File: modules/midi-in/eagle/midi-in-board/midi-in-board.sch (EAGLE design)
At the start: 20 parts, among them IC1 LM358N, T1 BC547, T2 BC547, X1 MIDI IN, X2 MIDI THRU

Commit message: Finish up midi in board schematic, for now
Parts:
- added C2, C3, C4, C5, C6, C7: 100n, rcl:C-EU050-024X044
- added IC2: TL072P, linear:TL072P
- added IC3, IC4: TL074P, linear:TL074P
- added JP1, JP2: (no value), pinhead:PINHD-1X8
- added JP3: (no value), pinhead:PINHD-1X1
- added JP4: (no value), pinhead:PINHD-1X7
- added JP5, JP6: (no value), pinhead:PINHD-1X2
- added R10, R12, R13, R14, R15, R16, R18, R20, R22, R24, R26, R27, R33, R35, R37, R39, R41, R49, R50, R9: 10K, rcl:R-EU_0207/7
- added R11: 1K, rcl:R-EU_0207/7
- added R17, R19, R21, R23, R25, R28, R29, R30, R31, R32: 100K, rcl:R-EU_0207/7
- added R34, R36, R38, R40, R42: 3.6K, rcl:R-EU_0207/7
- added R43, R44, R45, R46, R47, R51: 1K, pot:TRIM_EU-CA6V
- added R48: 20K, rcl:R-EU_0207/7
- added R52, R53: 220R, rcl:R-EU_0207/7
- added T3: BC547, transistor:BC547
- added X3: CHANNEL SELECT SW, con-molex:22-23-2021
- added X4: POWER IN, con-wago-500:W237-103
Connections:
- new net N$13: C3.1, R12.1, R17.1, SV2.12
- new net N$27: IC2A.-IN, R17.2, R28.1
- new net N$28: IC3A.-IN, R19.2, R29.1
- new net N$29: IC3C.-IN, R21.2, R30.1
- new net N$30: C2.2, R10.2, V11.!SRCLR, V21.!SRCLR
- new net N$31: IC4A.-IN, R23.2, R31.1
- new net N$32: IC4C.-IN, R25.2, R32.1
- new net N$33: IC2A.OUT, R18.1, R28.2
- new net N$34: IC2B.-IN, R18.2, R33.1
- new net N$35: IC3A.OUT, R20.1, R29.2
- new net N$36: IC3B.-IN, R20.2, R35.1
- new net N$37: IC3C.OUT, R22.1, R30.2
- new net N$38: IC3D.-IN, R22.2, R37.1
- new net N$39: IC4C.OUT, R27.1, R32.2
- new net N$40: IC4D.-IN, R27.2, R41.1
- new net N$41: IC2P.V-, IC3P.V-, X4-3.KL
- new net N$42: R50.2, R51.A
- new net N$43: IC4P.V-
- new net N$44: R48.1, R49.2
- new net N$45: R49.1, R51.E
- new net N$46: IC2A.+IN, IC3A.+IN, IC3C.+IN, IC4A.+IN, IC4C.+IN, R51.S
- new net N$48: JP1.1, V11.QA
- new net N$49: JP1.2, V11.QB
- new net N$50: JP1.3, V11.QC
- new net N$51: JP1.4, V11.QD
- new net N$52: JP1.5, V11.QE
- new net N$53: R33.2, R34.1
- new net N$54: JP1.6, V11.QF
- new net N$55: JP1.7, V11.QG
- new net N$56: R35.2, R36.1
- new net N$57: R37.2, R38.1
- new net N$58: JP1.8, V11.QH
- new net N$59: R39.2, R40.1
- new net N$60: JP2.1, V21.QA
- new net N$61: R41.2, R42.1
- new net N$62: R34.2, R43.E
- new net N$63: R36.2, R44.E
- new net N$64: R38.2, R45.E
- new net N$65: R40.2, R46.E
- new net N$66: R42.2, R47.E
- new net N$67: IC2B.OUT, JP4.3, R43.A
- new net N$68: IC3B.OUT, JP4.4, R44.A
- new net N$69: IC3D.OUT, JP4.5, R45.A
- new net N$70: IC4B.OUT, JP4.6, R46.A
- new net N$71: IC4D.OUT, JP4.7, R47.A
- new net N$72: JP2.2, V21.QB
- new net N$73: JP2.3, V21.QC
- new net N$74: JP2.4, V21.QD
- new net N$75: JP2.5, V21.QE
- new net N$76: JP2.6, V21.QF
- new net N$77: JP2.7, V21.QG
- new net N$78: JP2.8, V21.QH
- new net N$79: JP5.1, R52.2
- new net N$8: R9.1, T3.B
- new net N$80: JP6.1, R53.2
- new net V-: C1.1, C2.1, IC1P.V+, OK1.VCC, R11.2, R2.2, R3.2, R9.2, SV1.4, T1.C, T2.C, T3.C
- net GND: now also C3.2, C4.2, C5.2, C6.2, C7.2, IC2B.+IN, IC3B.+IN, IC3D.+IN, IC4B.+IN, IC4D.+IN, JP5.2, JP6.2, R10.1, R12.2, R13.2, R14.2, R15.2, R16.2, R50.1, T3.E, X3-2.S, X4-2.KL
- net N$10: now also IC4B.-IN, R24.2, R26.2, R39.1; no longer SV2.12
- net N$14: now also R11.1, X3-1.S
- net N$15: now also C4.1, R13.1, R19.1
- net N$16: now also C5.1, R14.1, R21.1
- net N$17: now also C6.1, R15.1, R23.1
- net N$18: now also C7.1, R16.1, R25.1
- net N$20: now also JP4.1, R52.1
- net N$22: now also JP4.2, R53.1
- net N$23: now also IC4A.OUT, R24.1, R26.1, R31.2; no longer V11.!SRCLR, V21.!SRCLR
- net VCC: now also IC2P.V+, IC3P.V+, IC4P.V+, JP3.1, R48.2, X4-1.KL; no longer C1.1, IC1P.V+, OK1.VCC, R2.2, R3.2, SV1.4, T1.C, T2.C
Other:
- note added: "+V"
- note added: "-V"
- note added: "DISP VCC"
- note added: "DISP1"
- note added: "DISP2"
- note added: "FRONT PANEL OUTPUTS"
- note added: "FreqCV OUT"
- note added: "GATE LED"
- note added: "GND"
- note added: "MIDI THRU INV BUFFER"
- note added: "MOD1 OUT"
- note added: "MOD2 OUT"
- note added: "MOD3 OUT"
- note added: "MOD4 OUT"
- note added: "OPAMP POWER"
- note added: "RESET ON POWER-UP"
- note added: "TRIGGER LED"
- moved on the sheet: C1, D1, IC1A, OK1, R1, R2, R3, R4, R5, R6, R7, R8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

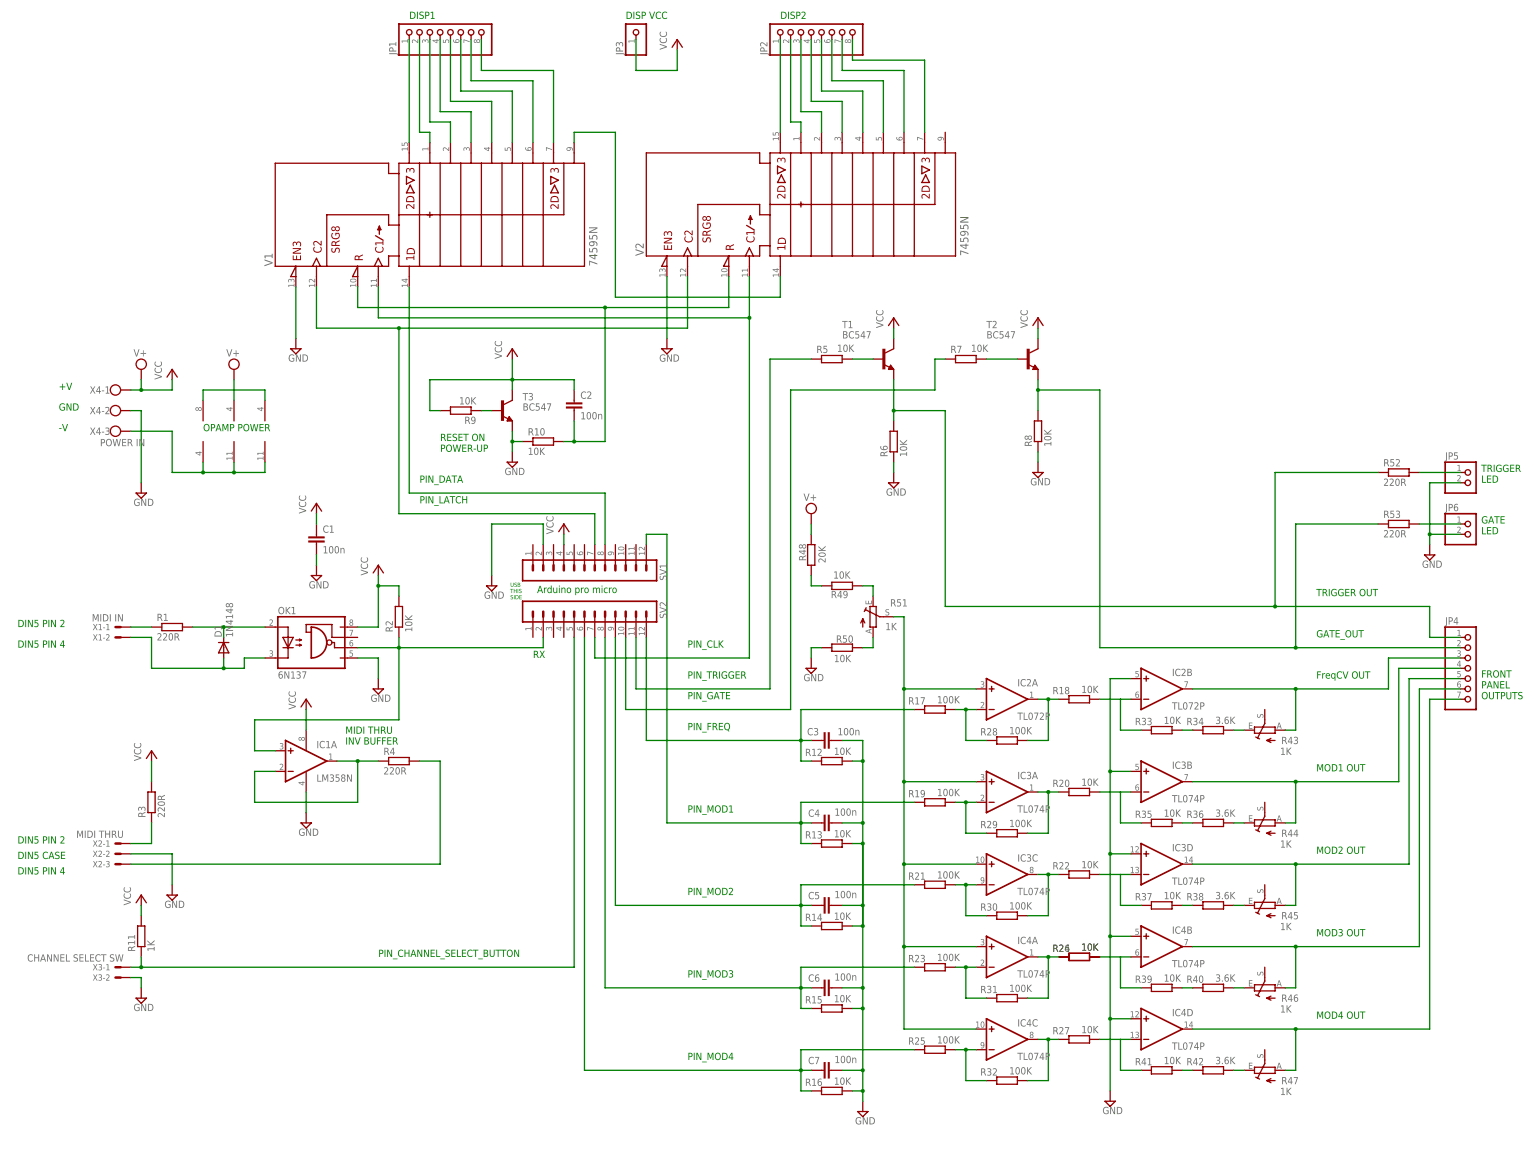
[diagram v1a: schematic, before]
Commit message: Start PCB design for main MIDI in board
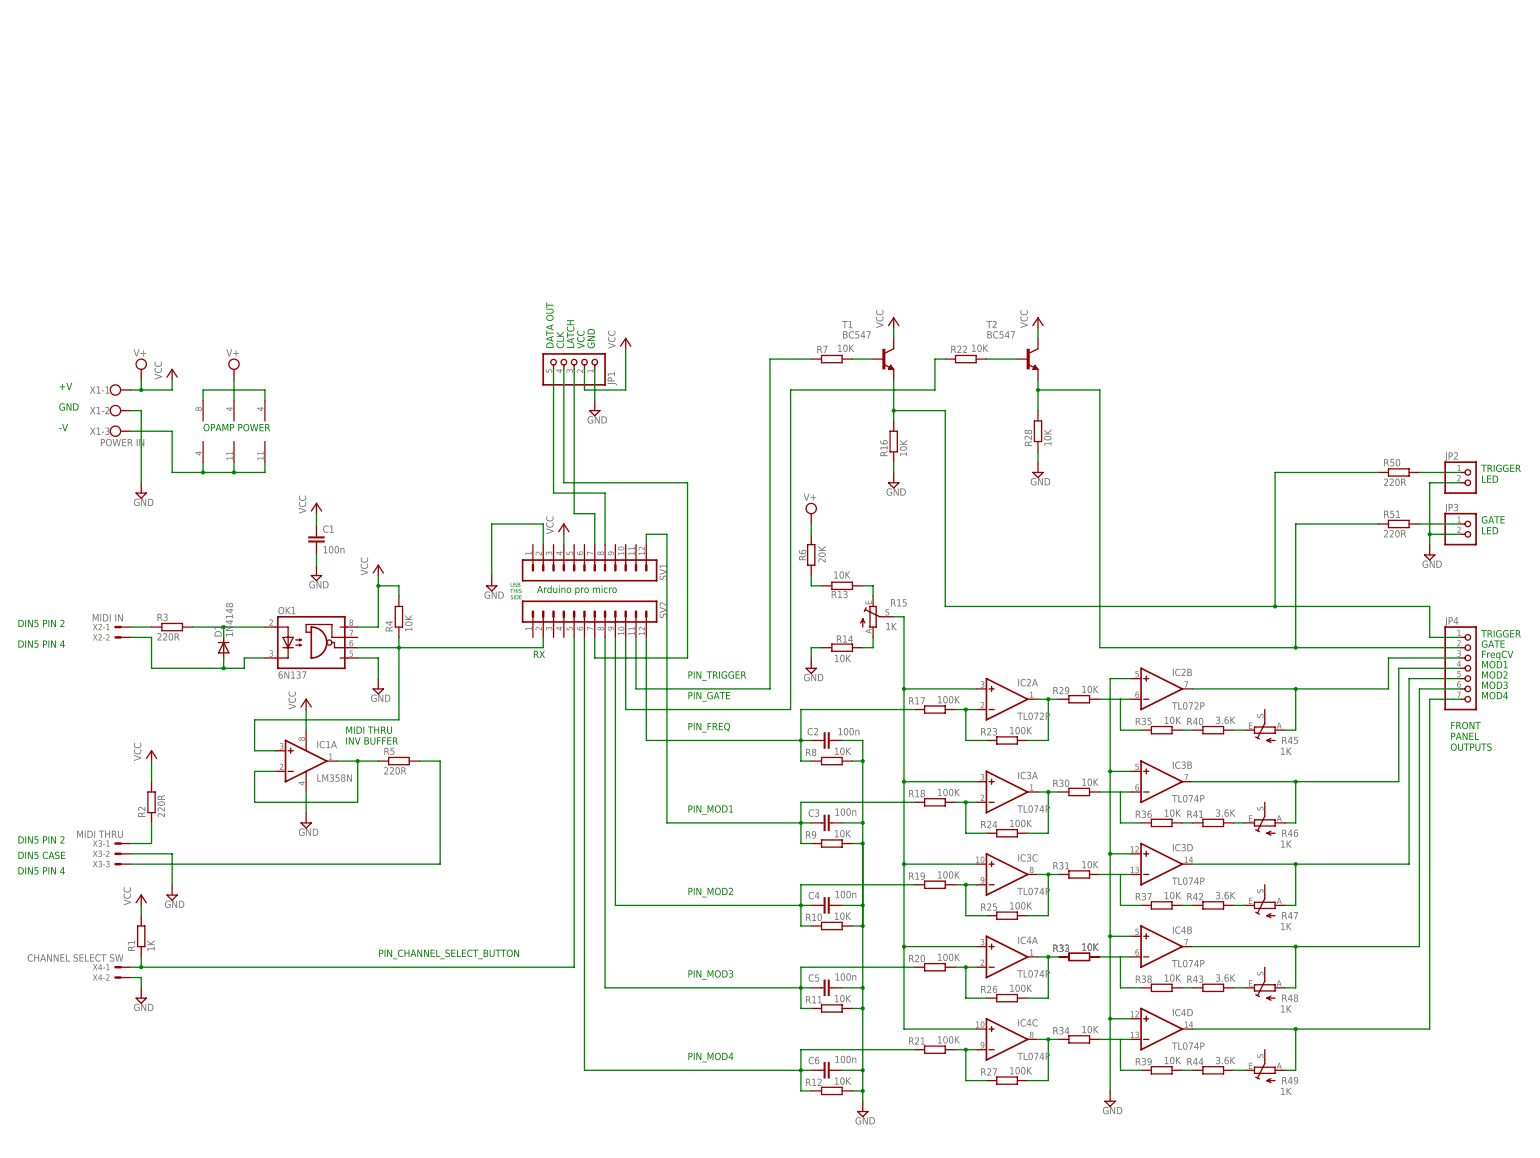
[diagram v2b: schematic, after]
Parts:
- removed C7: 100n, rcl:C-EU050-024X044
- removed JP5, JP6: (no value), pinhead:PINHD-1X2
- removed R52, R53: 220R, rcl:R-EU_0207/7
- removed T3: BC547, transistor:BC547
- removed V1, V2: 74595N, 74ttl-din:74595N
- JP1: device pinhead:PINHD-1X8 -> pinhead:PINHD-1X55X2MM
- JP2: device pinhead:PINHD-1X8 -> pinhead:PINHD-1X2
- JP3: device pinhead:PINHD-1X1 -> pinhead:PINHD-1X2
- R1: value 220R -> 1K
- R11: value 1K -> 10K
- R15, R49: value 10K -> 1K; device rcl:R-EU_0207/7 -> pot:TRIM_EU-CA6V
- R18, R20, R24, R26, R27: value 10K -> 100K
- R2, R5, R50: value 10K -> 220R
- R28, R29, R30, R31, R32: value 100K -> 10K
- R34, R36, R38: value 3.6K -> 10K
- R4: value 220R -> 10K
- R41: value 10K -> 3.6K
- R43, R44: value 1K -> 3.6K; device pot:TRIM_EU-CA6V -> rcl:R-EU_0207/7
- R48: value 20K -> 1K; device rcl:R-EU_0207/7 -> pot:TRIM_EU-CA6V
- R51: value 1K -> 220R; device pot:TRIM_EU-CA6V -> rcl:R-EU_0207/7
- R6: value 10K -> 20K
- X1: value MIDI IN -> POWER IN; device con-molex:22-23-2021 -> con-wago-500:W237-103
- X2: value MIDI THRU -> MIDI IN; device con-molex:22-23-2031 -> con-molex:22-23-2021
- X3: value CHANNEL SELECT SW -> MIDI THRU; device con-molex:22-23-2021 -> con-molex:22-23-2031
- X4: value POWER IN -> CHANNEL SELECT SW; device con-wago-500:W237-103 -> con-molex:22-23-2021
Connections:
- removed net N$1 (its old number): R1.1, X1-1.S
- removed net N$25: V11.QH*, V21.SER
- removed net N$30: C2.2, R10.2, V11.!SRCLR, V21.!SRCLR
- removed net N$48: JP1.1, V11.QA
- removed net N$49: JP1.2, V11.QB
- removed net N$50: JP1.3, V11.QC
- removed net N$51: JP1.4, V11.QD
- removed net N$52: JP1.5, V11.QE
- removed net N$54: JP1.6, V11.QF
- removed net N$55: JP1.7, V11.QG
- removed net N$58: JP1.8, V11.QH
- removed net N$60: JP2.1, V21.QA
- removed net N$64 (its old number): R38.2, R45.E
- removed net N$72: JP2.2, V21.QB
- removed net N$73: JP2.3, V21.QC
- removed net N$74: JP2.4, V21.QD
- removed net N$75: JP2.5, V21.QE
- removed net N$76: JP2.6, V21.QF
- removed net N$77: JP2.7, V21.QG
- removed net N$78: JP2.8, V21.QH
- removed net N$8: R9.1, T3.B
- removed net V-: C1.1, C2.1, IC1P.V+, OK1.VCC, R11.2, R2.2, R3.2, R9.2, SV1.4, T1.C, T2.C, T3.C
- new net N$6: R2.1, X3-1.S
- new net N$66: R44.2, R49.E
- net GND: now also C2.2, JP1.1, JP2.2, JP3.2, R10.2, R11.2, R14.1, R16.1, R28.1, R8.2, R9.2, X1-2.KL, X4-2.S; no longer C7.2, JP5.2, JP6.2, R10.1, R13.2, R14.2, R15.2, R16.2, R50.1, R6.1, R8.1, T3.E, V11.!G, V21.!G, X2-2.S, X4-2.KL
- net N$10: now also R32.2, R33.2, R38.1; no longer R24.2, R26.2, R39.1
- net N$11: now also R7.1; no longer R5.1
- net N$12: now also R22.1; no longer R7.1
- net N$13: now also C2.1, R8.1; no longer C3.1, R12.1
- net N$14: now also R1.1, X4-1.S; no longer R11.1, X3-1.S
- net N$15: now also C3.1, R18.1, R9.1; no longer C4.1, R13.1, R19.1
- net N$16: now also C4.1, R10.1, R19.1; no longer C5.1, R14.1, R21.1
- net N$17: now also C5.1, R11.1, R20.1; no longer C6.1, R15.1, R23.1
- net N$18: now also C6.1, R12.1, R21.1; no longer C7.1, R16.1, R25.1
- net N$19: now also R7.2; no longer R5.2
- net N$2: now also R3.2; no longer R1.2
- net N$20: now also R16.2, R50.1; no longer R52.1, R6.2
- net N$21: now also R22.2; no longer R7.2
- net N$22: now also R28.2, R51.1; no longer R53.1, R8.2
- net N$23: now also R26.2, R32.1, R33.1; no longer R24.1, R26.1, R31.2
- net N$24: now also JP1.4; no longer V11.SRCK, V21.SRCK
- net N$26: now also JP1.3; no longer V11.RCK, V21.RCK
- net N$27: now also R23.1; no longer R28.1
- net N$28: now also R18.2, R24.1; no longer R19.2, R29.1
- net N$29: now also R19.2, R25.1; no longer R21.2, R30.1
- net N$3: now also X2-2.S; no longer X1-2.S
- net N$31: now also R20.2, R26.1; no longer R23.2, R31.1
- net N$32: now also R21.2, R27.1; no longer R25.2, R32.1
- net N$33: now also R23.2, R29.1; no longer R18.1, R28.2
- net N$34: now also R29.2, R35.1; no longer R18.2, R33.1
- net N$35: now also R24.2, R30.1; no longer R20.1, R29.2
- net N$36: now also R30.2, R36.1; no longer R20.2, R35.1
- net N$37: now also R25.2, R31.1; no longer R22.1, R30.2
- net N$38: now also R31.2; no longer R22.2
- net N$39: now also R27.2, R34.1; no longer R27.1, R32.2
- net N$4: now also R5.1; no longer R4.1
- net N$40: now also R34.2, R39.1; no longer R27.2, R41.1
- net N$41: now also X1-3.KL; no longer X4-3.KL
- net N$42: now also R14.2, R15.A; no longer R50.2, R51.A
- net N$44: now also R13.2, R6.1; no longer R48.1, R49.2
- net N$45: now also R13.1, R15.E; no longer R49.1, R51.E
- net N$46: now also R15.S; no longer R51.S
- net N$5: now also R4.1; no longer R2.1
- net N$53: now also R35.2, R40.1; no longer R33.2, R34.1
- net N$56: now also R36.2, R41.1; no longer R35.2, R36.1
- net N$57: now also R42.1; no longer R38.1
- net N$59: now also R38.2, R43.1; no longer R39.2, R40.1
- net N$61: now also R39.2, R44.1; no longer R41.2, R42.1
- net N$62: now also R40.2, R45.E; no longer R34.2, R43.E
- net N$63: now also R41.2, R46.E; no longer R36.2, R44.E
- net N$65: now also R43.2, R48.E; no longer R40.2, R46.E
- net N$67: now also R45.A; no longer R43.A
- net N$68: now also R46.A; no longer R44.A
- net N$69: now also R47.A; no longer R45.A
- net N$7: now also R5.2, X3-3.S; no longer R4.2, X2-3.S
- net N$70: now also R48.A; no longer R46.A
- net N$71: now also R49.A; no longer R47.A
- net N$79: now also JP2.1, R50.2; no longer JP5.1, R52.2
- net N$80: now also JP3.1, R51.2; no longer JP6.1, R53.2
- net N$9: now also JP1.5; no longer V11.SER
- net VCC: now also C1.1, IC1P.V+, JP1.2, OK1.VCC, R1.2, R2.2, R4.2, R6.2, SV1.4, T1.C, T2.C, X1-1.KL; no longer JP3.1, R48.2, X4-1.KL
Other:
- note added: "CLK"
- note added: "DATA OUT"
- note added: "FreqCV"
- note added: "GATE"
- note added: "LATCH"
- note added: "MOD1"
- note added: "MOD2"
- note added: "MOD3"
- note added: "MOD4"
- note added: "TRIGGER"
- note added: "VCC"
- note removed: "DISP VCC"
- note removed: "DISP1"
- note removed: "DISP2"
- note removed: "FreqCV OUT"
- note removed: "GATE_OUT"
- note removed: "MOD1 OUT"
- note removed: "MOD2 OUT"
- note removed: "MOD3 OUT"
- note removed: "MOD4 OUT"
- note removed: "PIN_CLK"
- note removed: "PIN_DATA"
- note removed: "PIN_LATCH"
- note removed: "RESET ON POWER-UP"
- note removed: "TRIGGER OUT"
- moved on the sheet: C2, C3, C4, C5, C6, R1, R10, R11, R12, R13, R14, R16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
